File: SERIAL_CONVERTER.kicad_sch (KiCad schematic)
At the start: 0 parts

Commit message: Initial layout and all parts added. Some pins still not connected to power
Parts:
- added U2: 74LS125, Package_DIP:DIP-14_W7.62mm_SMDSocket_SmallPads, symbol 74xx:74LS125
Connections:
- new net +3V3: U2.14 (VCC)
- new net GND: U2.7 (GND)
- new net OE: U2.1
- new net OE_2: U2.4
- new net OE_3: U2.10
- new net OE_4: U2.13
- new net OUT: U2.3
- new net OUT_2: U2.6
- new net OUT_3: U2.8
- new net OUT_4: U2.11
- new net TX: U2.2
- new net TX_2: U2.5
- new net TX_3: U2.9
- new net TX_4: U2.12
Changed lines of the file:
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@@
 (kicad_sch (version 20210621) (generator eeschema)
   (paper "A4")
+  (wire (pts (xy 74.422 96.52) (xy 74.422 98.806))
+    (stroke (width 0) (type default) (color 0 0 0 0))
+  )
+  (wire (pts (xy 73.66 76.962) (xy 73.66 79.248))
+    (stroke (width 0) (type default) (color 0 0 0 0))
+  )
+  (wire (pts (xy 73.66 53.086) (xy 73.66 55.372))
+    (stroke (width 0) (type default) (color 0 0 0 0))
+  )
+  (wire (pts (xy 73.406 116.332) (xy 73.406 118.618))
+    (stroke (width 0) (type default) (color 0 0 0 0))
+  )
+  (hierarchical_label "OUT_2" (shape output) (at 73.66 79.248 0)
+    (effects (font (size 1.27 1.27)) (justify left))
+  )
+  (hierarchical_label "RX" (shape output) (at 73.66 53.086 0)
+    (effects (font (size 1.27 1.27)) (justify left))
+  )
+  (hierarchical_label "OE_3" (shape input) (at 66.802 102.87 180)
+    (effects (font (size 1.27 1.27)) (justify right))
+  )
+  (hierarchical_label "TX_2" (shape input) (at 58.42 76.962 180)
+    (effects (font (size 1.27 1.27)) (justify right))
+  )
+  (hierarchical_label "TX" (shape input) (at 58.42 53.086 180)
+    (effects (font (size 1.27 1.27)) (justify right))
+  )
+  (hierarchical_label "OE_2" (shape input) (at 66.04 83.312 180)
+    (effects (font (size 1.27 1.27)) (justify right))
+  )
+  (hierarchical_label "RX_2" (shape output) (at 73.66 76.962 0)
+    (effects (font (size 1.27 1.27)) (justify left))
+  )
+  (hierarchical_label "OE" (shape input) (at 66.04 59.436 270)
+    (effects (font (size 1.27 1.27)) (justify right))
+  )
+  (hierarchical_label "RX_4" (shape output) (at 73.406 116.332 0)
+    (effects (font (size 1.27 1.27)) (justify left))
+  )
+  (hierarchical_label "OUT_4" (shape output) (at 73.406 118.618 0)
+    (effects (font (size 1.27 1.27)) (justify left))
+  )
+  (hierarchical_label "OUT_3" (shape output) (at 74.422 98.806 0)
+    (effects (font (size 1.27 1.27)) (justify left))
+  )
+  (hierarchical_label "OE_4" (shape input) (at 65.786 122.682 180)
+    (effects (font (size 1.27 1.27)) (justify right))
+  )
+  (hierarchical_label "RX_3" (shape output) (at 74.422 96.52 0)
+    (effects (font (size 1.27 1.27)) (justify left))
+  )
+  (hierarchical_label "OUT" (shape output) (at 73.66 55.372 0)
+    (effects (font (size 1.27 1.27)) (justify left))
+  )
+  (hierarchical_label "TX_4" (shape input) (at 58.166 116.332 180)
+    (effects (font (size 1.27 1.27)) (justify right))
+  )
+  (hierarchical_label "TX_3" (shape input) (at 59.182 96.52 180)
+    (effects (font (size 1.27 1.27)) (justify right))
+  )
+  (symbol (lib_id "74xx:74LS125") (at 66.04 76.962 0) (unit 2)
+    (in_bom yes) (on_board yes)
+    (property "Reference" "U2" (id 0) (at 66.04 71.882 0))
+    (property "Value" "74LS125" (id 1) (at 66.04 69.85 0))
+    (property "Footprint" "Package_DIP:DIP-14_W7.62mm_SMDSocket_SmallPads" (id 2) (at 66.04 76.962 0)
+      (effects (font (size 1.27 1.27)) hide)
+    )
+    (property "Datasheet" "http://www.ti.com/lit/gpn/sn74LS125" (id 3) (at 66.04 76.962 0)
+      (effects (font (size 1.27 1.27)) hide)
+    )
+    (pin "4")
+    (pin "5")
+    (pin "6")
+  )
+  (symbol (lib_id "74xx:74LS125") (at 66.04 53.086 0) (unit 1)
+    (in_bom yes) (on_board yes)
+    (property "Reference" "U2" (id 0) (at 66.04 46.228 0))
+    (property "Value" "74LS125" (id 1) (at 66.04 42.926 0))
+    (property "Footprint" "Package_DIP:DIP-14_W7.62mm_SMDSocket_SmallPads" (id 2) (at 66.04 53.086 0)
+      (effects (font (size 1.27 1.27)) hide)
+    )
+    (property "Datasheet" "http://www.ti.com/lit/gpn/sn74LS125" (id 3) (at 66.04 53.086 0)
+      (effects (font (size 1.27 1.27)) hide)
+    )
+    (pin "1")
+    (pin "2")
+    (pin "3")
+  )
+  (symbol (lib_id "74xx:74LS125") (at 64.77 140.462 90) (unit 5)
+    (in_bom yes) (on_board yes) (fields_autoplaced)
+    (property "Reference" "U2" (id 0) (at 64.77 129.54 90))
+    (property "Value" "74LS125" (id 1) (at 64.77 132.08 90))
+    (property "Footprint" "Package_DIP:DIP-14_W7.62mm_SMDSocket_SmallPads" (id 2) (at 64.77 140.462 0)
+      (effects (font (size 1.27 1.27)) hide)
+    )
+    (property "Datasheet" "http://www.ti.com/lit/gpn/sn74LS125" (id 3) (at 64.77 140.462 0)
+      (effects (font (size 1.27 1.27)) hide)
+    )
+    (pin "14")
+    (pin "7")
+  )
+  (symbol (lib_id "power:GND") (at 77.47 140.462 90) (unit 1)
+    (in_bom yes) (on_board yes) (fields_autoplaced)
+    (property "Reference" "#PWR010" (id 0) (at 83.82 140.462 0)
+      (effects (font (size 1.27 1.27)) hide)
+    )
+    (property "Value" "GND" (id 1) (at 81.28 140.4619 90)
+      (effects (font (size 1.27 1.27)) (justify right))
+    )
+    (property "Footprint" "" (id 2) (at 77.47 140.462 0)
+      (effects (font (size 1.27 1.27)) hide)
+    )
+    (property "Datasheet" "" (id 3) (at 77.47 140.462 0)
+      (effects (font (size 1.27 1.27)) hide)
+    )
+    (pin "1")
+  )
+  (symbol (lib_id "power:+3.3V") (at 52.07 140.462 90) (unit 1)
+    (in_bom yes) (on_board yes) (fields_autoplaced)
+    (property "Reference" "#PWR09" (id 0) (at 55.88 140.462 0)
+      (effects (font (size 1.27 1.27)) hide)
+    )
+    (property "Value" "+3.3V" (id 1) (at 48.26 140.4619 90)
+      (effects (font (size 1.27 1.27)) (justify left))
+    )
+    (property "Footprint" "" (id 2) (at 52.07 140.462 0)
+      (effects (font (size 1.27 1.27)) hide)
+    )
+    (property "Datasheet" "" (id 3) (at 52.07 140.462 0)
+      (effects (font (size 1.27 1.27)) hide)
+    )
+    (pin "1")
+  )
+  (symbol (lib_id "74xx:74LS125") (at 65.786 116.332 0) (unit 4)
+    (in_bom yes) (on_board yes) (fields_autoplaced)
+    (property "Reference" "U2" (id 0) (at 65.786 106.68 0))
+    (property "Value" "74LS125" (id 1) (at 65.786 109.22 0))
+    (property "Footprint" "Package_DIP:DIP-14_W7.62mm_SMDSocket_SmallPads" (id 2) (at 65.786 116.332 0)
+      (effects (font (size 1.27 1.27)) hide)
+    )
+    (property "Datasheet" "http://www.ti.com/lit/gpn/sn74LS125" (id 3) (at 65.786 116.332 0)
+      (effects (font (size 1.27 1.27)) hide)
+    )
+    (pin "11")
+    (pin "12")
+    (pin "13")
+  )
+  (symbol (lib_id "74xx:74LS125") (at 66.802 96.52 0) (unit 3)
+    (in_bom yes) (on_board yes) (fields_autoplaced)
+    (property "Reference" "U2" (id 0) (at 66.802 87.63 0))
+    (property "Value" "74LS125" (id 1) (at 66.802 90.17 0))
+    (property "Footprint" "Package_DIP:DIP-14_W7.62mm_SMDSocket_SmallPads" (id 2) (at 66.802 96.52 0)
+      (effects (font (size 1.27 1.27)) hide)
+    )
+    (property "Datasheet" "http://www.ti.com/lit/gpn/sn74LS125" (id 3) (at 66.802 96.52 0)
+      (effects (font (size 1.27 1.27)) hide)
+    )
+    (pin "10")
+    (pin "8")
+    (pin "9")
+  )
 )

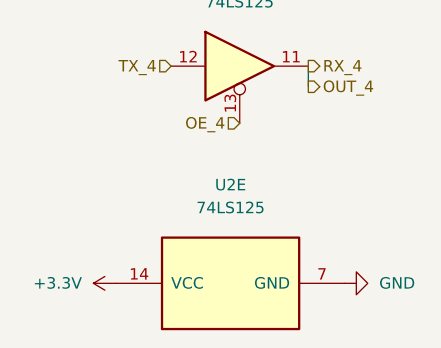
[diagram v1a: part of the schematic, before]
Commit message: Added usb to ethernet and changed mcu to stm32g4
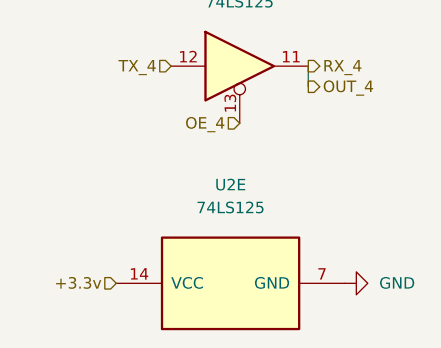
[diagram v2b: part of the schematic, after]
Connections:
- net +3V3 renamed +3.3v
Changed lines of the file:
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@@
     (effects (font (size 1.27 1.27)) (justify left))
+  )
+  (hierarchical_label "+3.3v" (shape input) (at 52.07 140.462 180)
+    (effects (font (size 1.27 1.27)) (justify right))
   )
   (hierarchical_label "OUT_3" (shape output) (at 74.422 98.806 0)
@@
       (effects (font (size 1.27 1.27)) hide)
     )
-    (pin "1")
-  )
-  (symbol (lib_id "power:+3.3V") (at 52.07 140.462 90) (unit 1)
-    (in_bom yes) (on_board yes) (fields_autoplaced)
-    (property "Reference" "#PWR09" (id 0) (at 55.88 140.462 0)
-      (effects (font (size 1.27 1.27)) hide)
-    )
-    (property "Value" "+3.3V" (id 1) (at 48.26 140.4619 90)
-      (effects (font (size 1.27 1.27)) (justify left))
-    )
-    (property "Footprint" "" (id 2) (at 52.07 140.462 0)
-      (effects (font (size 1.27 1.27)) hide)
-    )
-    (property "Datasheet" "" (id 3) (at 52.07 140.462 0)
-      (effects (font (size 1.27 1.27)) hide)
-    )
